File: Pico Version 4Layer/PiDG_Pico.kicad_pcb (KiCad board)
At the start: 4 copper layers, 126 x 126 mm, 79 parts, among them J1 Conn_02x05_Odd_Even, J10 Trig, J11 Laser Enable, J12 Pixel Reset, J14 Pico Socket A, J15 Pico Socket B, J16 Laser En/PWM Trig/GND, J17 USB-C PD in, J2 Conn_02x05_Odd_Even, J3 Conn_02x05_Odd_Even, J4 Conn_02x05_Odd_Even, J5 Conn_02x05_Odd_Even, J6 Conn_02x05_Odd_Even, J7 Laser 1, J8 Laser 2, U1 74LVC1G04, U10 74AHCT1G08, U12 74LVC1G17, U13 UCC27524, U14 CH224K, U15 AP63205WU, U16 LM66100, U17 LT3065EDD, U18 TPS3700DDC, U2 SN74LVC04AD, U3 74LVC1G04, U4 SN74LVC04AD, U5 74LVC1G04, U6 SN74LVC04AD, U7 74AHCT1G08, U8 74AHCT1G08, U9 NCP718xSN180

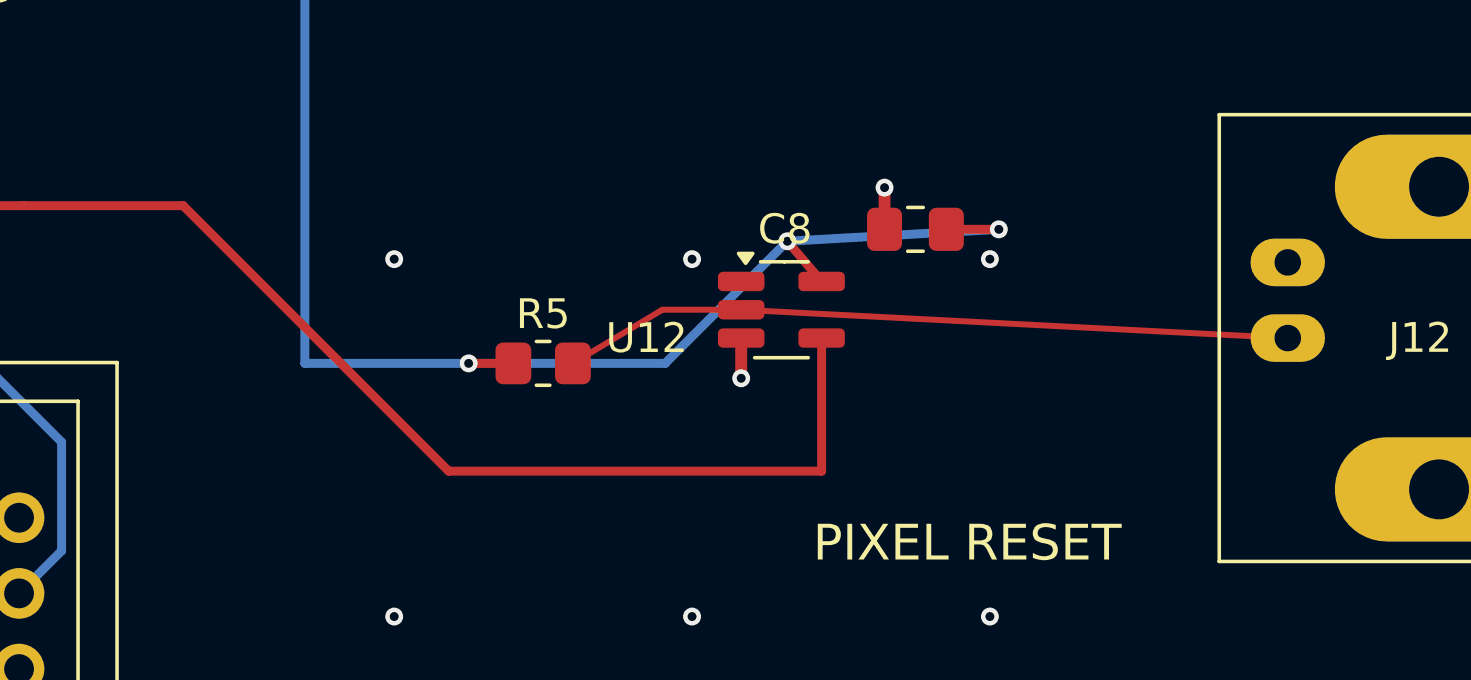
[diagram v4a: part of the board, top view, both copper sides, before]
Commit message: Tidy the U12 pixel-reset input cluster
The J12 -> U12 input ran as an 18 mm line at a slight angle, squeezed
between U12's pins 4 and 5, because U12's input faced away from the BNC.
C8 (U12's decoupling) sat 3 mm away and reached pin 5 through two vias,
and R5 hung off a dog-leg to the west.

- U12 rotated 180 degrees onto J12's centreline (y 120.65): PIXRST_IN is
  now one straight horizontal trace from U12 pin 2 to J12's centre pin.
- R5 (3k3 pull-up) sits on that line; C8 directly under U12 pin 5 with
  its own GND via; one +3V3 line C8 -> R5 fed by a single via from the
  B.Cu +3V3 trunk (was three vias).
- PIXRST leaves pin 4 horizontally into the existing 45-degree run.
- DRC 0 / 0 unconnected, parity unchanged; gerbers, drill, zip and both
  CPLs regenerated (BOMs unchanged).

Co-Authored-By: Claude Opus 5.5 (1M context) <noreply@anthropic.com>
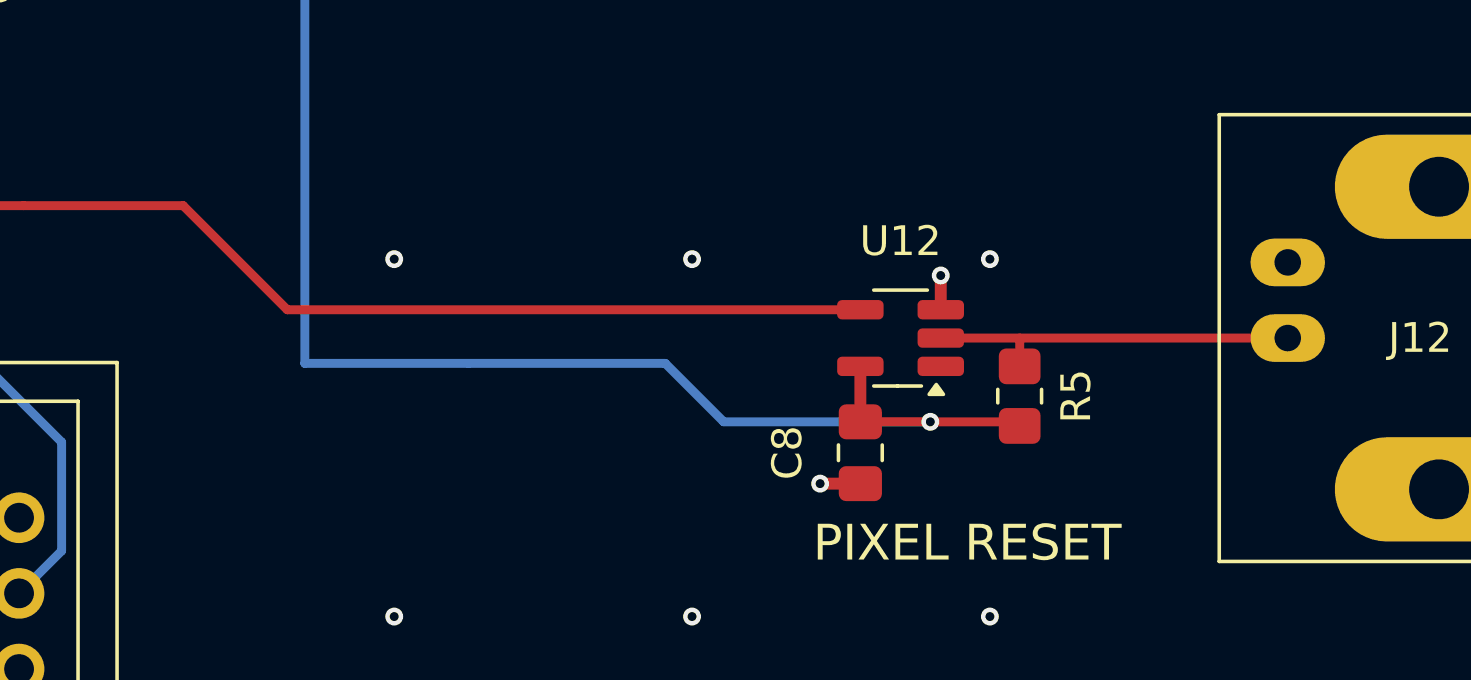
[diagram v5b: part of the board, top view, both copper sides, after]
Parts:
- moved R5 16.0 mm to (236.0, 122.6), turned to 90 degrees
- moved C8 7.72 mm to (230.7, 124.5), turned to -90 degrees
- moved U12 4.11 mm to (232.0, 120.7), turned to 180 degrees
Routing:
- net PIXRST_IN: track 24.5 -> 12.6 mm
- net PIXRST: track 67.1 -> 61.7 mm
- net +3V3: track 143.2 -> 142.2 mm, vias 4 -> 2

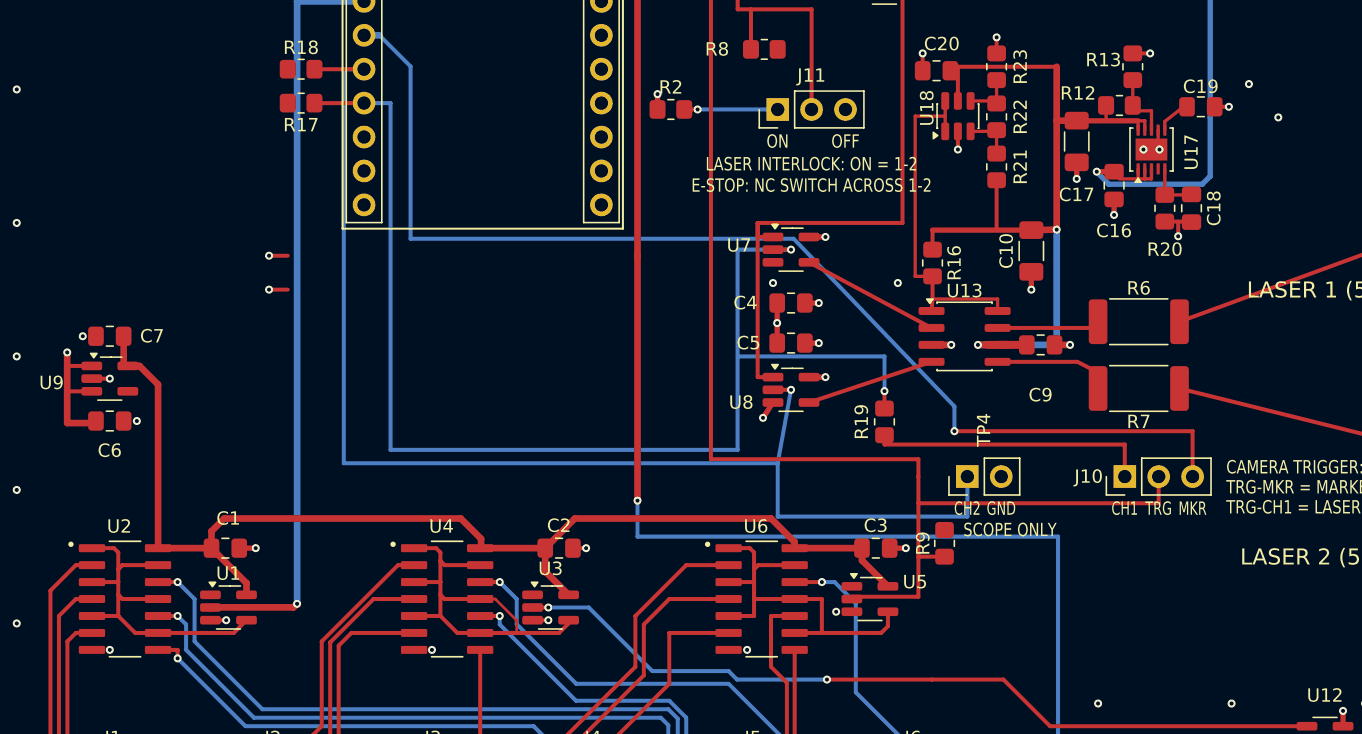
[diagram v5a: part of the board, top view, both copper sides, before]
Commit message: Remove three orphan GND vias; give seven pour-only returns a pad stub
- Removed the plane-only GND vias at (226.3, 71.6) and (228.5, 74.1),
  left over from the LP2951 layout, and (200.0, 86.5); no pad relies on
  them.
- Kept the seven vias that are the only ground vias for U2, U4, U6
  (camera line drivers), U5, U7 and U9's caps C6/C7. Removing them would
  have put U4/U6 ground 10-13 mm of pour from the plane. Each now has a
  straight 0.4 mm stub from its pad instead of relying on thermal spokes
  in the pour.
- Edge and SE-quadrant stitching unchanged.
- DRC 0 / 0 unconnected, parity unchanged; gerbers, drill and zip
  regenerated.

Co-Authored-By: Claude Opus 5.5 (1M context) <noreply@anthropic.com>
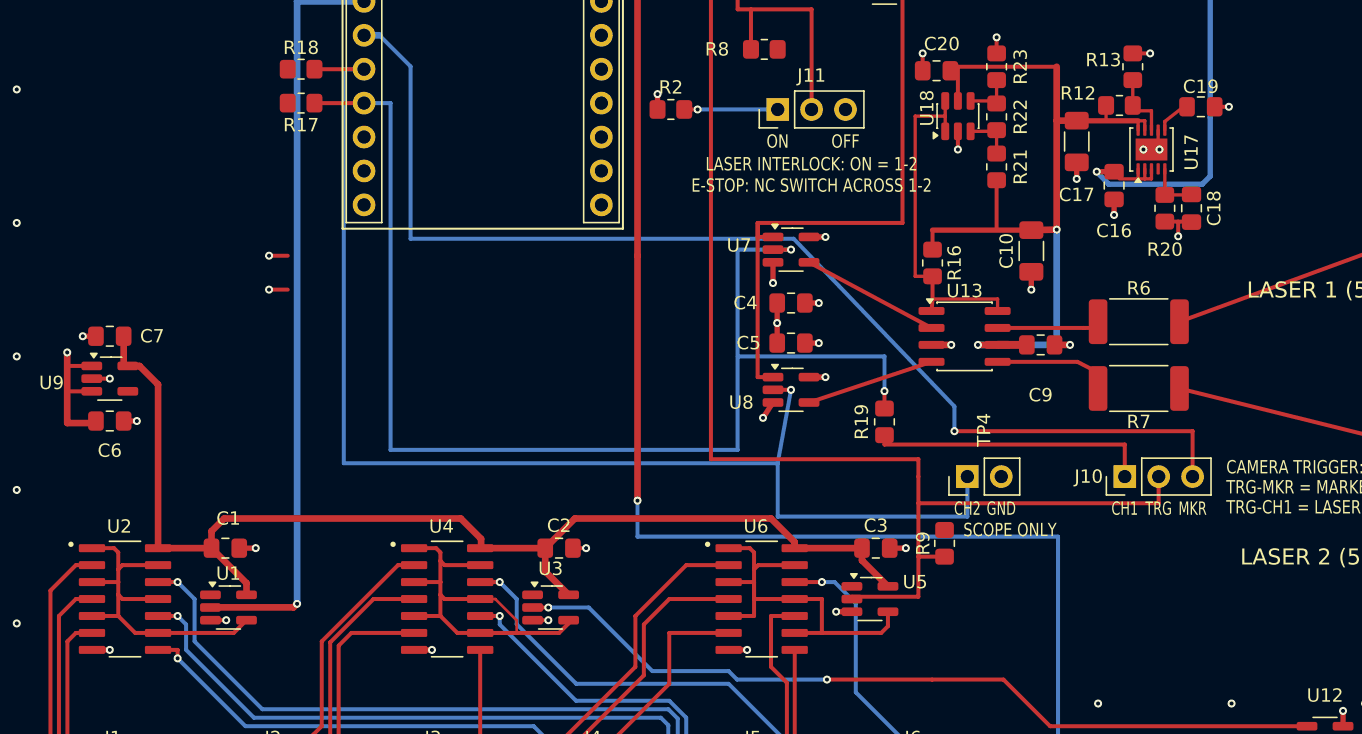
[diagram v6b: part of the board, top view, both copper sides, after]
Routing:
- net GND: track 57.6 -> 66.4 mm, vias 93 -> 90
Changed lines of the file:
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@@
+	)
+	(segment
+		(start 142.0075 96.8375)
+		(end 142.995 96.8375)
+		(width 0.4)
+		(layer "F.Cu")
+		(net "GND")
 	)
 	(segment
@@
 	)
 	(segment
+		(start 196.56 111.1225)
+		(end 195.38 111.1225)
+		(width 0.4)
+		(layer "F.Cu")
+		(net "GND")
+	)
+	(segment
 		(start 226.5625 47.3)
 		(end 226.5625 49.2)
@@
 	)
 	(segment
+		(start 139.9325 90.4875)
+		(end 138.945 90.4875)
+		(width 0.4)
+		(layer "F.Cu")
+		(net "GND")
+	)
+	(segment
+		(start 139.635 113.9825)
+		(end 140.97 113.9825)
+		(width 0.4)
+		(layer "F.Cu")
+		(net "GND")
+	)
+	(segment
 		(start 223.7375 73.3)
 		(end 224.8 73.3)
@@
 	)
 	(segment
+		(start 190.65 84.95)
+		(end 190.65 86.5)
+		(width 0.4)
+		(layer "F.Cu")
+		(net "GND")
+	)
+	(segment
 		(start 210 85.6625)
 		(end 210 87)
@@
 	)
 	(segment
+		(start 187.325 113.9825)
+		(end 188.71 113.9825)
+		(width 0.4)
+		(layer "F.Cu")
+		(net "GND")
+	)
+	(segment
 		(start 236.9 47.2375)
 		(end 236.9 48.7)
@@
 	)
 	(segment
+		(start 163.765 113.9825)
+		(end 165.1 113.9825)
+		(width 0.4)
+		(layer "F.Cu")
+		(net "GND")
+	)
+	(segment
 		(start 216.2 80.2375)
 		(end 216.2 81.4)
@@
 	)
 	(via
-		(at 188.71 113.982)
+		(at 188.71 113.9825)
 		(size 0.6)
 		(drill 0.3)
@@
 	)
 	(via
-		(at 140.97 113.982)
+		(at 140.97 113.9825)
 		(size 0.6)
 		(drill 0.3)
@@
 	)
 	(via
-		(at 195.38 111.125)
+		(at 195.38 111.1225)
 		(size 0.6)
 		(drill 0.3)
@@
 	)
 	(via
-		(at 165.1 113.982)
+		(at 165.1 113.9825)
 		(size 0.6)
 		(drill 0.3)
@@
 	)
 	(via
-		(at 226.3 71.6)
-		(size 0.6)
-		(drill 0.3)
-		(layers "F.Cu" "B.Cu")
-		(net "GND")
-	)
-	(via
 		(at 202 32)
 		(size 0.6)
@@
 		(size 0.6)
 		(drill 0.3)
-		(layers "F.Cu" "B.Cu")
-		(net "GND")
-	)
-	(via
-		(at 228.5 74.095)
-		(size 0.6)
-		(drill 0.3)
-		(layers "F.Cu" "B.Cu")
-		(net "GND")
-	)
-	(via
-		(at 200 86.5)
-		(size 0.6)
-		(drill 0.3)

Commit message: Move J16 to the top edge, between the Pico and J17
J16 (EN in / TRIG out / GND right-angle header) moves from the right
edge next to the BNCs to the top edge between the Pico and the USB-C
input, pins pointing off the board with the same 2.1 mm overhang as TP3.

- Pads at x 187.8 / 190.34 / 192.88, y 38 (rot 90).
- TRIG comes straight up x 186 and over pad 1 into pad 2; EN comes up
  x 199 and under pads 3/2 into pad 1. All top layer, no vias, no
  crossings. The runs out to the right edge are gone: PWM_TRIG_TAP
  172 -> 122 mm, LASER_EN_TAP 67 -> 44 mm.
- Silkscreen: EN / TRIG / GND under the pins and a four-line key below
  (NEVER FIT A SHUNT, EN IN pull low = lasers off, TRIG OUT monitor,
  NOT FAIL-SAFE: E-STOP ON J11), reworded to fit between the Pico and
  the USB-PD block.
- DRC 0 / 0 unconnected, parity unchanged; gerbers, drill, zip and both
  CPLs regenerated; README (map, connector table), Hardware.md,
  JLC_ORDER.md enclosure notes and the BOM's R19 note updated.

Co-Authored-By: Claude Opus 5.5 (1M context) <noreply@anthropic.com>
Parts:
- moved J16 64.5 mm to (187.8, 38.0), turned to 90 degrees
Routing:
- net PWM_TRIG_TAP: track 172.2 -> 122.2 mm
- net LASER_EN_TAP: track 67.0 -> 44.2 mm
- net GND: track 66.4 -> 66.7 mm, vias 90 -> 81
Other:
- board text added: "EN"
- board text added: "EN IN: PULL LOW = LASERS OFF"
- board text added: "NOT FAIL-SAFE: E-STOP ON J11"
- board text added: "TRIG"
- board text removed: "ENABLE IN: PULL LOW = LASERS OFF"
- board text removed: "NOT FAIL-SAFE - PUT THE E-STOP ON J11"

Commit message: Pixel-reset gate: optional camera pixel reset between pulse pairs
The Pico can now hold every camera's pixels in reset (TDRSTN low)
between pulse pairs, like a shutter, while the J12 BNC input keeps
working exactly as before.

Board
- U3 74LVC1G04 -> 74LVC1G00 (NAND, same SOT-23-5 footprint): through U4
  the cameras get TDRSTN = J12 input AND PIXRST_GATE, so either source
  resets the pixels.
- PIXRST_GATE = Pico GP16 (J15 pad 20) -> U3 pin 1 (previously NC), with
  R24 10k pull-up to +3V3 so the gate reads "no reset" unless driven low.
  Routed F.Cu from J15 pad 20, one B.Cu 45-degree hop, into U3 pad 1.
- ERC 0, DRC 0 / 0 unconnected, no real parity net conflicts; gerbers,
  drill, zip, CPLs and BOMs regenerated (U3 = SN74LVC1G00DBVR C7826;
  R24 joins the 10k line). 76 parts, 41 JLC lines.

Firmware
- PIXGATE 0|1|2 (off / while ARMED / always), PIXLEAD ns (pixels
  released this long before CH1, >= 5 cycles), PIXLAG ns (reset again
  this long after the last laser pulse). Validated on realized cycles:
  PIXLEAD + DELAY + WIDTH + PIXLAG <= 1/FREQ - 3 cycles.
- pio0 SM3 runs the existing pulse program on GP16 with the pad output
  inverted (GPIO_OVERRIDE_INVERT), enabled on the same cycle as CH1/CH2/
  MARKER; a stopped gate leaves the pixels free. SYNC moved to pio1 to
  free SM3 (the Pico 2 W's CYW43 driver takes pio2).
- STATUS reports PIXRESET (reset length per period, its start after CH1,
  and the free window); HELP documents the commands.
- tools/timing_check/check_pixgate.py: 1600 random sets against an
  exact model plus a cycle-level PIO simulation of CH1/CH2/gate
  (513 gated, 0 mismatches; mutation-tested). All existing checks give
  their unchanged expected counts. Strict-warning builds clean.

Docs: README (commands, PIXGATE section, STATUS, troubleshooting),
Hardware.md (pin map, pixel-reset chain, gate timing), JLC_ORDER.md.

Co-Authored-By: Claude Opus 5.5 (1M context) <noreply@anthropic.com>
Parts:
- added R24: 10k, Resistor_SMD:R_0805_2012Metric_Pad1.20x1.40mm_HandSolder, F.Cu at (178.8, 96.0)
- U3: value 74LVC1G04 -> 74LVC1G00
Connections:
- J15 pad 20: (no net) -> PIXRST_GATE
- U3 pad 1: unconnected-(U3-NC-Pad1) -> PIXRST_GATE
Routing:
- net PIXRST_GATE: track 0.00 -> 31.3 mm, vias 0 -> 2
- net +3V3: track 142.2 -> 142.9 mm
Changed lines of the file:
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@@
 			(layers "*.Cu" "*.Mask")
 			(remove_unused_layers no)
+			(net "PIXRST_GATE")
 		)
 		(embedded_fonts no)
@@
 			)
 		)
-		(property "Value" "74LVC1G04"
+		(property "Value" "74LVC1G00"
 			(at 1.27 3.175 0)
 			(layer "F.Fab")
@@
 			)
 		)
-		(property "Datasheet" "https://www.ti.com/lit/ds/symlink/sn74lvc1g04.pdf"
+		(property "Datasheet" "https://www.ti.com/lit/ds/symlink/sn74lvc1g00.pdf"
 			(at 0 0 0)
 			(unlocked yes)
@@
 			)
 		)
-		(property "Description" "Single NOT Gate, Low-Voltage CMOS"
+		(property "Description" "Pixel-reset combiner (1.8 V): NAND of PIXRST (J12 via U12) and PIXRST_GATE (Pico GP16); through U4 the cameras see TDRSTN = PIXRST AND GATE"
 			(at 0 0 0)
 			(unlocked yes)
@@
 			(layers "F.Cu" "F.Mask" "F.Paste")
 			(roundrect_rratio 0.25)
-			(net "unconnected-(U3-NC-Pad1)")
+			(net "PIXRST_GATE")
 			(pinfunction "NC")
 			(pintype "no_connect")
@@
 		)
 	)
+	(footprint "Resistor_SMD:R_0805_2012Metric_Pad1.20x1.40mm_HandSolder"
+		(layer "F.Cu")
+		(at 178.795 96 180)
+		(descr "Resistor SMD 0805 (2012 Metric), square (rectangular) end terminal, IPC-7351 nominal with elongated pad for handsoldering. (Body size source: IPC-SM-782 page 72, https://www.pcb-3d.com/wordpress/wp-content/uploads/ipc-sm-782a_amendment_1_and_2.pdf)")
+		(tags "resistor handsolder")
+		(property "Reference" "R24"
+			(at 0 1.7 0)
+			(layer "F.SilkS")
+			(effects
+				(font
+					(size 1 1)
+					(thickness 0.15)
+				)
+			)
+		)
+		(property "Value" "10k"
+			(at 0 1.65 180)
+			(layer "F.Fab")
+			(effects
+				(font
+					(size 1 1)
+					(thickness 0.15)
+				)
+			)
+		)
+		(property "Datasheet" ""
+			(at 0 0 180)
+			(layer "F.Fab")
+			(hide yes)
+			(effects
+				(font
+					(size 1.27 1.27)
+				)
+			)
+		)
+		(property "Description" "PIXRST_GATE pull-up: gate high (no pixel reset) unless the Pico drives it low"
+			(at 0 0 180)
+			(layer "F.Fab")
+			(hide yes)
+			(effects
+				(font
+					(size 1.27 1.27)
+				)
+			)
+		)
+		(property "KiLib_Generator" "SMD_2terminal_chip_molded"
+			(at 0 0 180)
+			(layer "F.SilkS")
+			(hide yes)
+			(effects
+				(font
+					(size 1 1)
+					(thickness 0.15)
+				)
+			)
+		)
+		(attr smd)
+		(duplicate_pad_numbers_are_jumpers no)
+		(fp_line
+			(start -0.227064 0.735)
+			(end 0.227064 0.735)
+			(stroke
+				(width 0.12)
+				(type solid)
+			)
+			(layer "F.SilkS")
+		)
+		(fp_line
+			(start -0.227064 -0.735)
+			(end 0.227064 -0.735)
+			(stroke
+				(width 0.12)
+				(type solid)
+			)
+			(layer "F.SilkS")
+		)
+		(fp_rect
+			(start -1.85 -0.95)
+			(end 1.85 0.95)
+			(stroke
+				(width 0.05)
+				(type solid)
+			)
+			(fill no)
+			(layer "F.CrtYd")
+		)
+		(fp_rect
+			(start -1 -0.625)
+			(end 1 0.625)
+			(stroke
+				(width 0.1)
+				(type solid)
+			)
+			(fill no)
+			(layer "F.Fab")
+		)
+		(fp_text user "${REFERENCE}"
+			(at 0 0 180)
+			(layer "F.Fab")
+			(effects
+				(font
+					(size 0.5 0.5)
+					(thickness 0.08)
+				)
+			)
+		)
+		(pad "1" smd roundrect
+			(at -1 0 180)
+			(size 1.2 1.4)
+			(layers "F.Cu" "F.Mask" "F.Paste")
+			(roundrect_rratio 0.208333)
+			(net "+3V3")
+		)
+		(pad "2" smd roundrect
+			(at 1 0 180)
+			(size 1.2 1.4)
+			(layers "F.Cu" "F.Mask" "F.Paste")
+			(roundrect_rratio 0.208333)
+			(net "PIXRST_GATE")
+		)
+		(embedded_fonts no)
+		(model "${KICAD10_3DMODEL_DIR}/Resistor_SMD.3dshapes/R_0805_2012Metric.step"
+			(offset
+				(xyz 0 0 0)
+			)
+			(scale
+				(xyz 1 1 1)
+			)
+			(rotate
+				(xyz 0 0 0)
+			)
+		)
+	)
 	(gr_line
 		(start 158.405 30.63)
@@
 	)
 	(segment
+		(start 179.795 96)
+		(end 180.5 96)
+		(width 0.3)
+		(layer "F.Cu")
+		(net "+3V3")
+	)
+	(segment
 		(start 180.5 42.545)
 		(end 180.5 84.455)
@@
 	)
 	(segment
+		(start 172.64 108.155)
+		(end 172.64 109.858)
+		(width 0.3)
+		(layer "F.Cu")
+		(net "PIXRST_GATE")
+	)
+	(segment
+		(start 177.795 80.645)
+		(end 177.795 101.8)
+		(width 0.3)
+		(layer "F.Cu")
+		(net "PIXRST_GATE")
+	)
+	(via
+		(at 172.64 108.155)
+		(size 0.6)
+		(drill 0.3)
+		(layers "F.Cu" "B.Cu")
+		(net "PIXRST_GATE")
+	)
+	(via
+		(at 177.795 101.8)
+		(size 0.6)
+		(drill 0.3)
+		(layers "F.Cu" "B.Cu")
+		(net "PIXRST_GATE")
+	)
+	(segment
+		(start 177.795 101.8)
+		(end 177.795 103)
+		(width 0.3)
+		(layer "B.Cu")
+		(net "PIXRST_GATE")
+	)
+	(segment
+		(start 177.795 103)
+		(end 172.64 108.155)
+		(width 0.3)
+		(layer "B.Cu")
+		(net "PIXRST_GATE")
+	)
+	(segment
